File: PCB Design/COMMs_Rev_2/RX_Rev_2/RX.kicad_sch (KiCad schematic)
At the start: 50 parts, among them J1 Conn_01x24_Pin, J2 Conn_01x24_Pin, J3 Conn_01x03_Pin, J4 Conn_01x04_Pin, J5 Conn_01x02_Pin, U1 TLV9101IDCKR, U2 TPD2E007DCKR, U3 INA828IDR, U4 OPA2322AIDGKR

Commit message: Initial PCB Placement
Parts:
- removed TP6: TestPoint, TestPoint:TestPoint_Pad_1.0x1.0mm, symbol Connector:TestPoint
- added R22, R23: 100k, Resistor_SMD:R_0603_1608Metric, symbol Device:R_US
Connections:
- net AGND: now also R22.2, R23.1
- net RX_N: now also R23.2
- net RX_P: now also R22.1

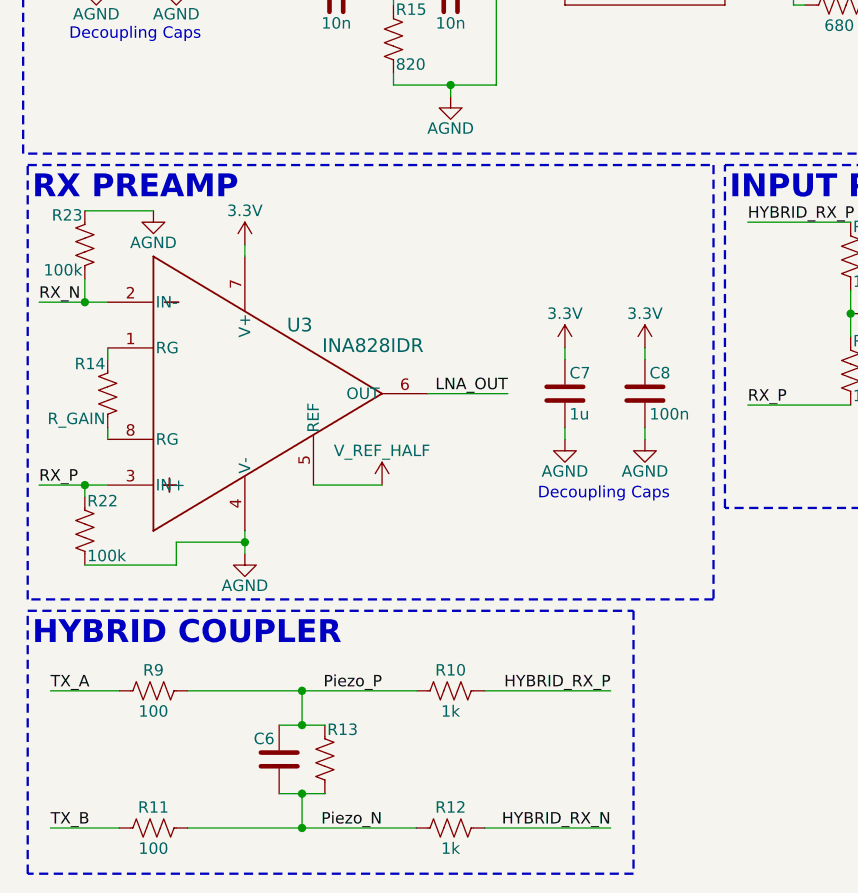
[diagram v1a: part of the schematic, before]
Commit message: RX_Rev_2 schematic design review fixes
- Set R14 gain resistor to calculated value for target INA828 gain
- Resolved C6 ambiguity (marked DNP)
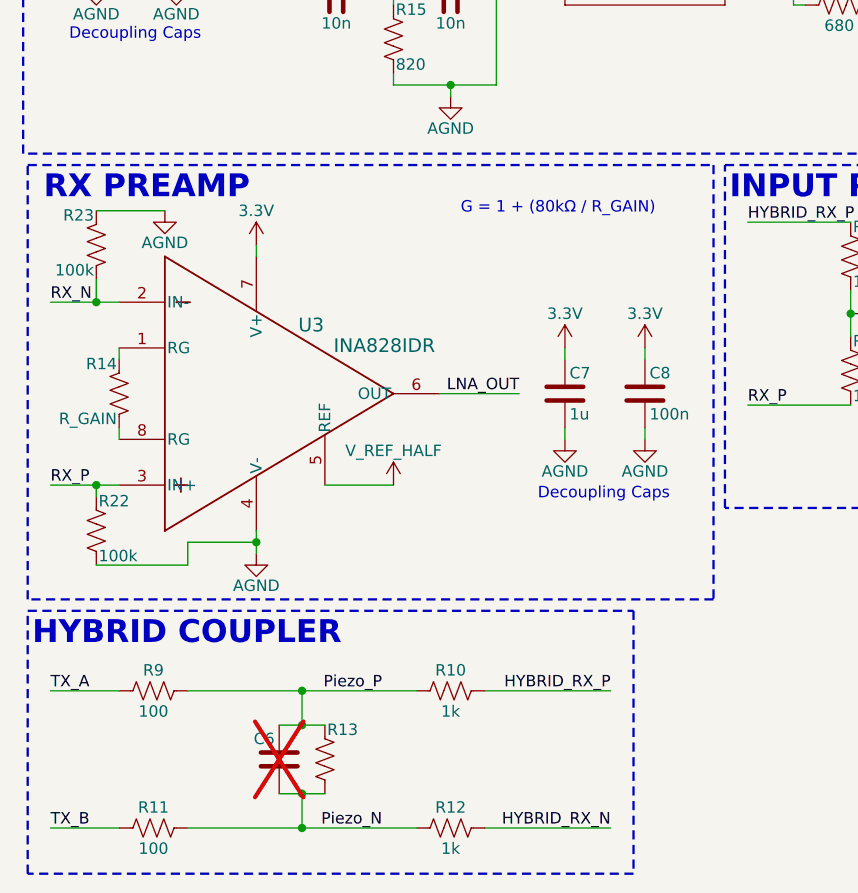
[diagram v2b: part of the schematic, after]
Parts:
- C6: now not fitted
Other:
- note added: "G = 1 + (80kΩ / R_GAIN)"
- moved on the sheet: R14, R22, R23, U3

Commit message: Small Updates
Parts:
- R13: now not fitted
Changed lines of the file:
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@@
 		(in_bom yes)
 		(on_board yes)
-		(dnp no)
+		(dnp yes)
 		(property "Reference" "R13"
 			(at 47.244 157.988 0)

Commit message: Added Title Summary and Updated Rev 2.1
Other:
- company: (none) -> Capstone
- title: (none) -> SWARM RX COMMs
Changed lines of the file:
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@@
 	(generator_version "9.0")
 	(paper "A4")
+	(title_block
+		(title "SWARM RX COMMs")
+		(date "2026-03-23")
+		(rev "2.1")
+		(company "Capstone")
+		(comment 1 "By SAMANTHA CHONG")
+	)
 	(rectangle
 		(start 203.2 62.23)

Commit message: Updated RX
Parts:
- C6, R13: value ~ -> (none)

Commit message: Updated
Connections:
- net AGND: no longer R22.2, R23.1
- net V_REF_HALF: now also R22.2, R23.1
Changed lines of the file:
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@@
 	)
 	(junction
-		(at 39.37 137.16)
-		(diameter 0)
-		(color 0 0 0 0)
-	)
-	(junction
 		(at 64.77 69.85)
 		(diameter 0)
@@
 	(wire
 		(pts
-			(xy 39.37 135.89) (xy 39.37 137.16)
+			(xy 39.37 135.89) (xy 39.37 138.43)
 		)
 		(stroke
@@
 	(wire
 		(pts
-			(xy 31.75 137.16) (xy 39.37 137.16)
-		)
-		(stroke
-			(width 0)
-			(type default)
-		)
-	)
-	(wire
-		(pts
 			(xy 45.72 35.56) (xy 45.72 43.18)
 		)
@@
 	(wire
 		(pts
-			(xy 39.37 137.16) (xy 39.37 138.43)
-		)
-		(stroke
-			(width 0)
-			(type default)
-		)
-	)
-	(wire
-		(pts
 			(xy 153.67 20.32) (xy 162.56 20.32)
 		)
@@
 	(wire
 		(pts
-			(xy 31.75 139.7) (xy 31.75 137.16)
-		)
-		(stroke
-			(width 0)
-			(type default)
-		)
-	)
-	(wire
-		(pts
 			(xy 275.59 88.9) (xy 275.59 85.09)
 		)
@@
 	)
 	(symbol
-		(lib_id "power:GND")
-		(at 29.21 100.33 0)
-		(unit 1)
-		(body_style 1)
-		(exclude_from_sim no)
-		(in_bom yes)
-		(on_board yes)
-		(in_pos_files yes)
-		(dnp no)
-		(property "Reference" "#PWR037"
-			(at 29.21 106.68 0)
-			(hide yes)
-			(show_name no)
-			(do_not_autoplace no)
-			(effects
-				(font
-					(size 1.27 1.27)
-				)
-			)
-		)
-		(property "Value" "AGND"
-			(at 29.21 103.886 0)
-			(show_name no)
-			(do_not_autoplace no)
-			(effects
-				(font
-					(size 1.27 1.27)
-				)
-			)
-		)
-		(property "Footprint" ""
-			(at 29.21 100.33 0)
-			(hide yes)
-			(show_name no)
-			(do_not_autoplace no)
-			(effects
-				(font
-					(size 1.27 1.27)
-				)
-			)
-		)
-		(property "Datasheet" ""
-			(at 29.21 100.33 0)
-			(hide yes)
-			(show_name no)
-			(do_not_autoplace no)
-			(effects
-				(font
-					(size 1.27 1.27)
-				)
-			)
-		)
-		(property "Description" "Power symbol creates a global label with name \"GND\" , ground"
-			(at 29.21 100.33 0)
-			(hide yes)
-			(show_name no)
-			(do_not_autoplace no)
-			(effects
-				(font
-					(size 1.27 1.27)
-				)
-			)
-		)
-		(pin "1"
-		)
-		(instances
-			(project "RX"
-				(path "/487393bf-b13e-4fd8-b19d-84bece8bafcd"
-					(reference "#PWR037")
-					(unit 1)
-				)
-			)
-		)
-	)
-	(symbol
 		(lib_id "power:VCC")
 		(at 240.03 21.59 270)
@@
 	)
 	(symbol
+		(lib_id "power:VCC")
+		(at 31.75 139.7 180)
+		(unit 1)
+		(body_style 1)
+		(exclude_from_sim no)
+		(in_bom yes)
+		(on_board yes)
+		(in_pos_files yes)
+		(dnp no)
+		(property "Reference" "#PWR038"
+			(at 31.75 135.89 0)
+			(hide yes)
+			(show_name no)
+			(do_not_autoplace no)
+			(effects
+				(font
+					(size 1.27 1.27)
+				)
+			)
+		)
+		(property "Value" "V_REF_HALF"
+			(at 24.892 141.732 0)
+			(show_name no)
+			(do_not_autoplace no)
+			(effects
+				(font
+					(size 1.27 1.27)
+				)
+			)
+		)
+		(property "Footprint" ""
+			(at 31.75 139.7 0)
+			(hide yes)
+			(show_name no)
+			(do_not_autoplace no)
+			(effects
+				(font
+					(size 1.27 1.27)
+				)
+			)
+		)
+		(property "Datasheet" ""
+			(at 31.75 139.7 0)
+			(hide yes)
+			(show_name no)
+			(do_not_autoplace no)
+			(effects
+				(font
+					(size 1.27 1.27)
+				)
+			)
+		)
+		(property "Description" "Power symbol creates a global label with name \"VCC\""
+			(at 31.75 139.7 0)
+			(hide yes)
+			(show_name no)
+			(do_not_autoplace no)
+			(effects
+				(font
+					(size 1.27 1.27)
+				)
+			)
+		)
+		(pin "1"
+		)
+		(instances
+			(project "RX"
+				(path "/487393bf-b13e-4fd8-b19d-84bece8bafcd"
+					(reference "#PWR038")
+					(unit 1)
+				)
+			)
+		)
+	)
+	(symbol
 		(lib_id "Device:R_US")
 		(at 110.49 72.39 90)
@@
 					(unit 1)
 				)
+			)
+		)
+	)
+	(symbol
+		(lib_id "power:VCC")
+		(at 29.21 100.33 180)
+		(unit 1)
+		(body_style 1)
+		(exclude_from_sim no)
+		(in_bom yes)
+		(on_board yes)
+		(in_pos_files yes)
+		(dnp no)
+		(property "Reference" "#PWR037"
+			(at 29.21 96.52 0)
+			(hide yes)
+			(show_name no)
+			(do_not_autoplace no)
+			(effects
+				(font
+					(size 1.27 1.27)
+				)
+			)
+		)
+		(property "Value" "V_REF_HALF"
+			(at 29.21 104.14 0)
+			(show_name no)
+			(do_not_autoplace no)
+			(effects
+				(font
+					(size 1.27 1.27)
+				)
+			)
+		)
+		(property "Footprint" ""
+			(at 29.21 100.33 0)
+			(hide yes)
+			(show_name no)
+			(do_not_autoplace no)
+			(effects
+				(font
+					(size 1.27 1.27)
+				)
+			)
+		)
+		(property "Datasheet" ""
+			(at 29.21 100.33 0)
+			(hide yes)
+			(show_name no)
+			(do_not_autoplace no)
+			(effects
+				(font
+					(size 1.27 1.27)
+				)
+			)
+		)
+		(property "Description" "Power symbol creates a global label with name \"VCC\""
+			(at 29.21 100.33 0)
+			(hide yes)
+			(show_name no)
+			(do_not_autoplace no)
+			(effects
+				(font
+					(size 1.27 1.27)
+				)
+			)
+		)
+		(pin "1"
+		)
+		(instances
+			(project "RX"
+				(path "/487393bf-b13e-4fd8-b19d-84bece8bafcd"
+					(reference "#PWR037")
+					(unit 1)
+				)

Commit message: Revert "Updated"
This reverts commit 89be44ed720659141c8ee702c54a520a60db740f.
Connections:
- net AGND: now also R22.2, R23.1
- net V_REF_HALF: no longer R22.2, R23.1
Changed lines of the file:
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@@
 	)
 	(junction
+		(at 39.37 137.16)
+		(diameter 0)
+		(color 0 0 0 0)
+	)
+	(junction
 		(at 64.77 69.85)
 		(diameter 0)
@@
 	(wire
 		(pts
-			(xy 39.37 135.89) (xy 39.37 138.43)
+			(xy 39.37 135.89) (xy 39.37 137.16)
 		)
 		(stroke
@@
 	(wire
 		(pts
+			(xy 31.75 137.16) (xy 39.37 137.16)
+		)
+		(stroke
+			(width 0)
+			(type default)
+		)
+	)
+	(wire
+		(pts
 			(xy 45.72 35.56) (xy 45.72 43.18)
 		)
@@
 	(wire
 		(pts
+			(xy 39.37 137.16) (xy 39.37 138.43)
+		)
+		(stroke
+			(width 0)
+			(type default)
+		)
+	)
+	(wire
+		(pts
 			(xy 153.67 20.32) (xy 162.56 20.32)
 		)
@@
 	(wire
 		(pts
+			(xy 31.75 139.7) (xy 31.75 137.16)
+		)
+		(stroke
+			(width 0)
+			(type default)
+		)
+	)
+	(wire
+		(pts
 			(xy 275.59 88.9) (xy 275.59 85.09)
 		)
@@
 	)
 	(symbol
+		(lib_id "power:GND")
+		(at 29.21 100.33 0)
+		(unit 1)
+		(body_style 1)
+		(exclude_from_sim no)
+		(in_bom yes)
+		(on_board yes)
+		(in_pos_files yes)
+		(dnp no)
+		(property "Reference" "#PWR037"
+			(at 29.21 106.68 0)
+			(hide yes)
+			(show_name no)
+			(do_not_autoplace no)
+			(effects
+				(font
+					(size 1.27 1.27)
+				)
+			)
+		)
+		(property "Value" "AGND"
+			(at 29.21 103.886 0)
+			(show_name no)
+			(do_not_autoplace no)
+			(effects
+				(font
+					(size 1.27 1.27)
+				)
+			)
+		)
+		(property "Footprint" ""
+			(at 29.21 100.33 0)
+			(hide yes)
+			(show_name no)
+			(do_not_autoplace no)
+			(effects
+				(font
+					(size 1.27 1.27)
+				)
+			)
+		)
+		(property "Datasheet" ""
+			(at 29.21 100.33 0)
+			(hide yes)
+			(show_name no)
+			(do_not_autoplace no)
+			(effects
+				(font
+					(size 1.27 1.27)
+				)
+			)
+		)
+		(property "Description" "Power symbol creates a global label with name \"GND\" , ground"
+			(at 29.21 100.33 0)
+			(hide yes)
+			(show_name no)
+			(do_not_autoplace no)
+			(effects
+				(font
+					(size 1.27 1.27)
+				)
+			)
+		)
+		(pin "1"
+		)
+		(instances
+			(project "RX"
+				(path "/487393bf-b13e-4fd8-b19d-84bece8bafcd"
+					(reference "#PWR037")
+					(unit 1)
+				)
+			)
+		)
+	)
+	(symbol
 		(lib_id "power:VCC")
 		(at 240.03 21.59 270)
@@
 	)
 	(symbol
-		(lib_id "power:VCC")
-		(at 31.75 139.7 180)
-		(unit 1)
-		(body_style 1)
-		(exclude_from_sim no)
-		(in_bom yes)
-		(on_board yes)
-		(in_pos_files yes)
-		(dnp no)
-		(property "Reference" "#PWR038"
-			(at 31.75 135.89 0)
-			(hide yes)
-			(show_name no)
-			(do_not_autoplace no)
-			(effects
-				(font
-					(size 1.27 1.27)
-				)
-			)
-		)
-		(property "Value" "V_REF_HALF"
-			(at 24.892 141.732 0)
-			(show_name no)
-			(do_not_autoplace no)
-			(effects
-				(font
-					(size 1.27 1.27)
-				)
-			)
-		)
-		(property "Footprint" ""
-			(at 31.75 139.7 0)
-			(hide yes)
-			(show_name no)
-			(do_not_autoplace no)
-			(effects
-				(font
-					(size 1.27 1.27)
-				)
-			)
-		)
-		(property "Datasheet" ""
-			(at 31.75 139.7 0)
-			(hide yes)
-			(show_name no)
-			(do_not_autoplace no)
-			(effects
-				(font
-					(size 1.27 1.27)
-				)
-			)
-		)
-		(property "Description" "Power symbol creates a global label with name \"VCC\""
-			(at 31.75 139.7 0)
-			(hide yes)
-			(show_name no)
-			(do_not_autoplace no)
-			(effects
-				(font
-					(size 1.27 1.27)
-				)
-			)
-		)
-		(pin "1"
-		)
-		(instances
-			(project "RX"
-				(path "/487393bf-b13e-4fd8-b19d-84bece8bafcd"
-					(reference "#PWR038")
-					(unit 1)
-				)
-			)
-		)
-	)
-	(symbol
 		(lib_id "Device:R_US")
 		(at 110.49 72.39 90)
@@
 					(unit 1)
 				)
-			)
-		)
-	)
-	(symbol
-		(lib_id "power:VCC")
-		(at 29.21 100.33 180)
-		(unit 1)
-		(body_style 1)
-		(exclude_from_sim no)
-		(in_bom yes)
-		(on_board yes)
-		(in_pos_files yes)
-		(dnp no)
-		(property "Reference" "#PWR037"
-			(at 29.21 96.52 0)
-			(hide yes)
-			(show_name no)
-			(do_not_autoplace no)
-			(effects
-				(font
-					(size 1.27 1.27)
-				)
-			)
-		)
-		(property "Value" "V_REF_HALF"
-			(at 29.21 104.14 0)
-			(show_name no)
-			(do_not_autoplace no)
-			(effects
-				(font
-					(size 1.27 1.27)
-				)
-			)
-		)
-		(property "Footprint" ""
-			(at 29.21 100.33 0)
-			(hide yes)
-			(show_name no)
-			(do_not_autoplace no)
-			(effects
-				(font
-					(size 1.27 1.27)
-				)
-			)
-		)
-		(property "Datasheet" ""
-			(at 29.21 100.33 0)
-			(hide yes)
-			(show_name no)
-			(do_not_autoplace no)
-			(effects
-				(font
-					(size 1.27 1.27)
-				)
-			)
-		)
-		(property "Description" "Power symbol creates a global label with name \"VCC\""
-			(at 29.21 100.33 0)
-			(hide yes)
-			(show_name no)
-			(do_not_autoplace no)
-			(effects
-				(font
-					(size 1.27 1.27)
-				)
-			)
-		)
-		(pin "1"
-		)
-		(instances
-			(project "RX"
-				(path "/487393bf-b13e-4fd8-b19d-84bece8bafcd"
-					(reference "#PWR037")
-					(unit 1)
-				)
